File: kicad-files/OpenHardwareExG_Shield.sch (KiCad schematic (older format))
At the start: 189 parts, among them P1 CONN_1, P10 CONN_18, P11 CONN_1, P12 CONN_1, P13 CONN_1, P14 CONN_1, P15 CONN_1, P16 CONN_1, P17 CONN_1, P18 CONN_1, P19 ARDUINO_SHIELD, P2 CONN_1, P20 CONN_3X2, P21 CONN_3X2, P22 CONN_7, P23 CONN_1, P24 CONN_1, P25 CONN_1, P26 CONN_1, P27 CONN_1, P28 CONN_1, P29 CONN_1, P3 CONN_1, P30 CONN_1, P31 CONN_1, P32 CONN_1, P33 CONN_1, P34 CONN_1, P35 CONN_1, P36 CONN_1, P37 CONN_1, P38 CONN_1, P39 CONN_1, P4 CONN_1, P40 CONN_1, P41 CONN_1, P42 CONN_1, P43 CONN_1, P44 CONN_1, P45 CONN_1, P46 CONN_1, P47 CONN_1, P48 CONN_1, P49 CONN_1, P5 CONN_1, P50 CONN_1, P51 CONN_1, P52 CONN_1, P53 CONN_1, P54 CONN_1, P55 CONN_1, P6 CONN_1, P7 CONN_1, P8 CONN_1, P9 CONN_1, U1 ADS1299, U2 Z0109MNT1G, U3 TL431BIDBZR, U4 873-AAT3220IGY-33T1, U5 ADUM6000, U6 SI8663, U7 74LS02, U8 74LS00, U9 74LS125

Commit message: fix the crowbar on schematic
PCB still needs fixing
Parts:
- added C73: 330uF, ~, symbol CP
- C43: value 10uF -> 100nF
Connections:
- wire segments 765 -> 615
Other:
- note added: "5.5V Crowbar circuit"
- note removed: "3.8V Crowbar circuit"

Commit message: add footprint to 330uF C73
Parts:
- C73: footprint ~ -> c_tant_E

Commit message: T49D337K010ATE150 is a "D" footprint, not "E"
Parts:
- C73: footprint c_tant_E -> c_tant_D
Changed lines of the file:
@@
 Sheet 1 1
 Title ""
-Date "14 aug 2015"
+Date "30 aug 2015"
 Rev ""
 Comp ""
@@
 F 0 "C73" H 20750 1850 40  0000 L CNN
 F 1 "330uF" H 20750 1650 40  0000 L CNN
-F 2 "c_tant_E" H 20800 1600 30  0001 C CNN
+F 2 "c_tant_D" H 20800 1600 30  0001 C CNN
 F 3 "~" H 20700 1750 300 0000 C CNN
 	1    20700 1750

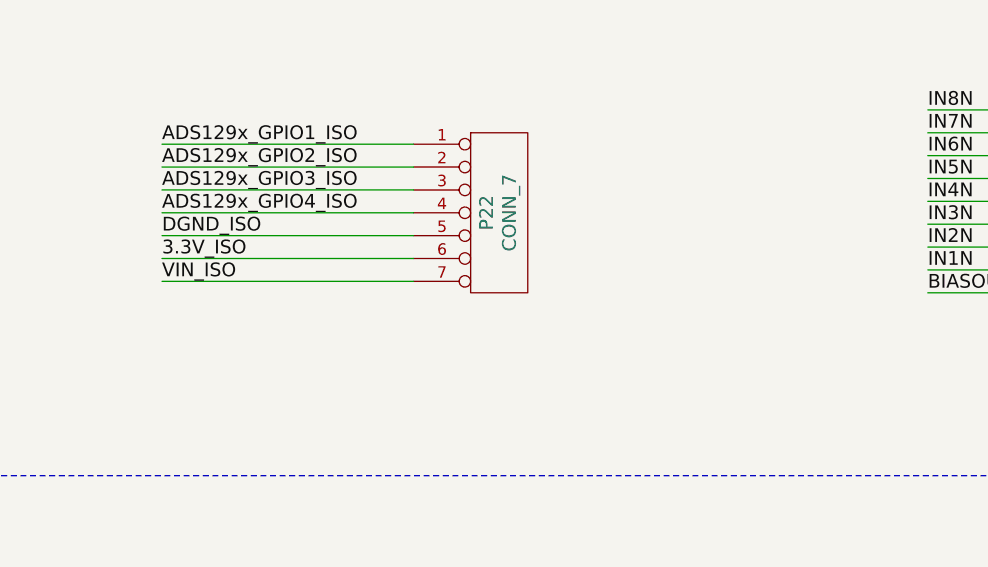
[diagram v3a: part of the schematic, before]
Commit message: add note to recommend female header for GPIO (P22)
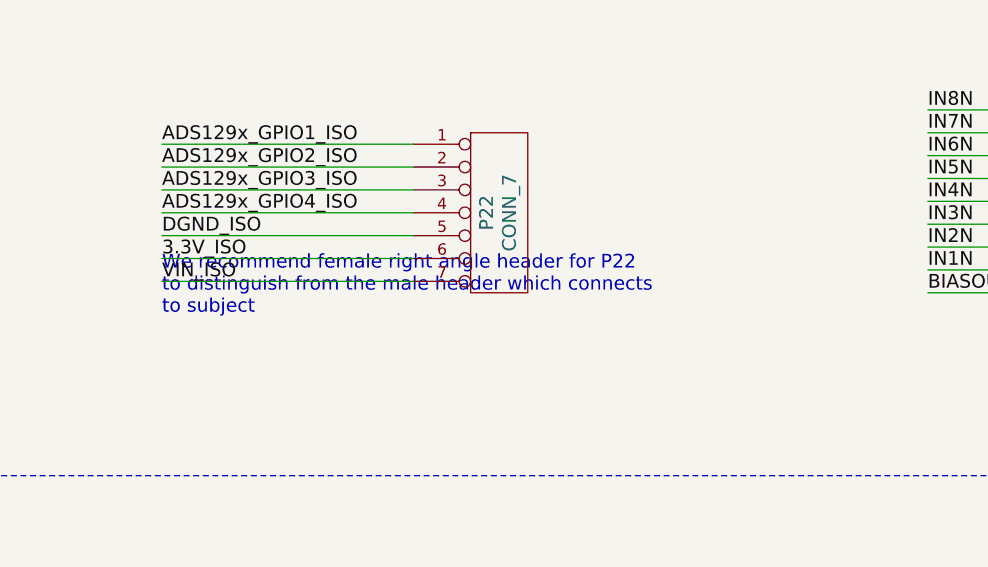
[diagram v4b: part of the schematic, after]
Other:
- note added: "We recommend female right angle header for P22\nto distinguish from the male header which connects\nto subject"
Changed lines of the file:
@@
 	20700 1950 20700 3000
 Connection ~ 20700 3000
+Text Notes 18850 10600 0    60   ~ 0
+We recommend female right angle header for P22\nto distinguish from the male header which connects\nto subject
 $EndSCHEMATC

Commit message: fix C43 footprint
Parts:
- C43: footprint SM0805 -> SM0603
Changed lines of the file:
@@
 F 0 "C43" H 15250 6900 50  0000 L CNN
 F 1 "100nF" H 15250 6700 50  0000 L CNN
-F 2 "SM0805" H 15250 6800 50  0001 C CNN
+F 2 "SM0603" H 15250 6800 50  0001 C CNN
 F 3 "" H 15200 6800 60  0001 C CNN
 	1    15200 6800

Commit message: connect DGND_ISO to DGND (DOH!); convert to KiCad 4
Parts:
- C1, C10, C11, C12, C13, C14, C15, C16, C17, C18, C19, C2, C20, C21, C22, C23, C24, C25, C26, C27, C28, C29, C3, C30, C31, C32, C33, C34, C35, C36, C37, C38, C39, C4, C40, C42, C43, C44, C45, C46, C47, C48, C49, C5, C50, C51, C52, C53, C54, C55, C56, C57, C58, C59, C6, C60, C61, C62, C63, C64, C65, C66, C67, C68, C69, C7, C70, C71, C72, C8, C9: symbol C -> C-RESCUE-OpenHardwareExG_Shield
- C41, C73: symbol CP -> CP-RESCUE-OpenHardwareExG_Shield
- D1: symbol LED -> LED-RESCUE-OpenHardwareExG_Shield
- R1, R10, R11, R12, R13, R14, R15, R16, R17, R18, R19, R2, R20, R21, R22, R23, R24, R25, R26, R27, R28, R29, R3, R30, R31, R32, R33, R34, R35, R36, R39, R4, R40, R41, R42, R43, R44, R45, R46, R5, R6, R7, R8, R9: symbol R -> R-RESCUE-OpenHardwareExG_Shield
- U5: symbol ADUM6000 -> ADuM6000
- U6: symbol SI8663 -> Si8663

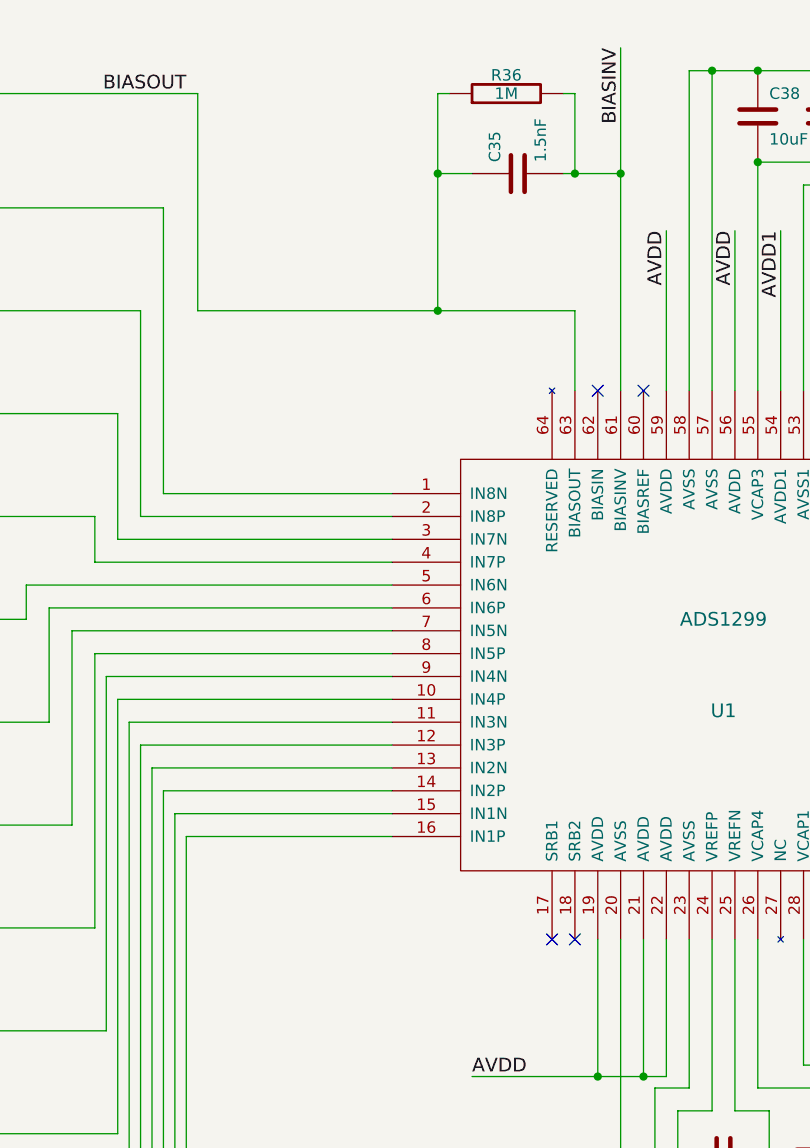
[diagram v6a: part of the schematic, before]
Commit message: add notes about connecting test points for next rev
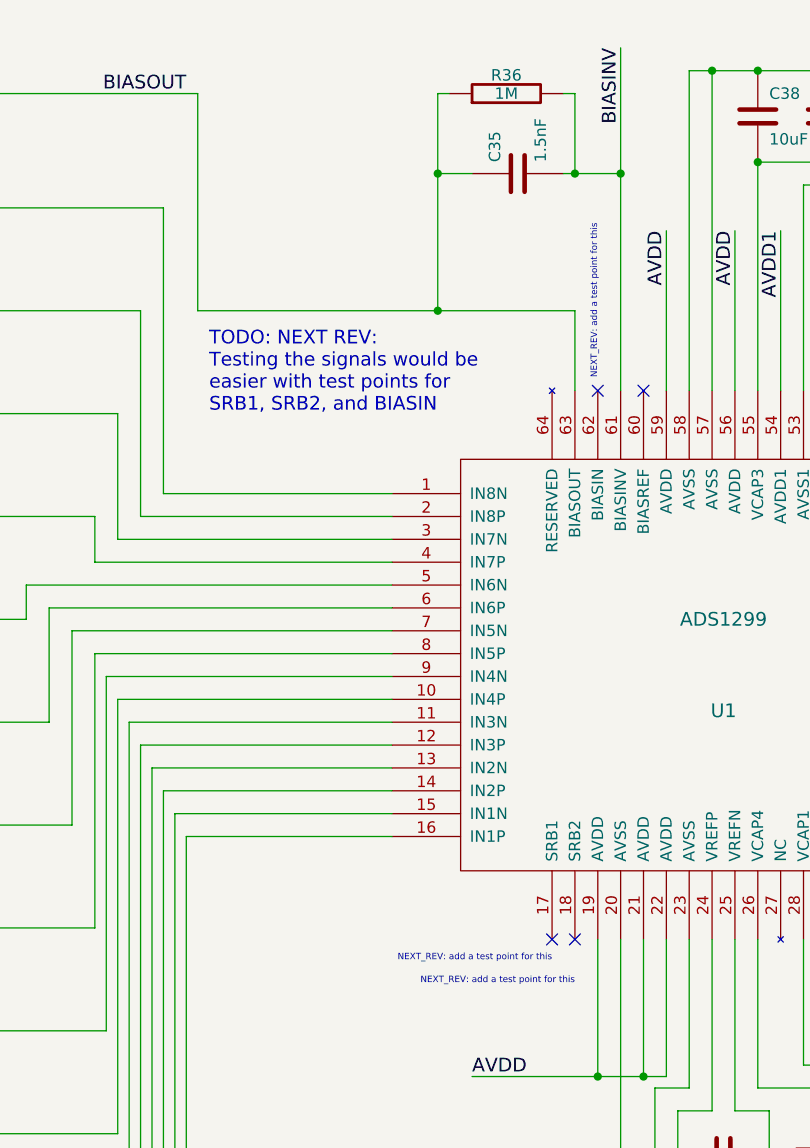
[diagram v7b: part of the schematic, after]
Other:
- note added: "NEXT_REV: add a test point for this"
- note added: "TODO: NEXT REV:\nTesting the signals would be\neasier with test points for\nSRB1, SRB2, and BIASIN"
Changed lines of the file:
@@
 Wire Wire Line
 	17750 7050 19750 7050
+Text Notes 10500 3150 1    28   ~ 0
+NEXT_REV: add a test point for this
+Text Notes 10300 5700 2    28   ~ 0
+NEXT_REV: add a test point for this
+Text Notes 10400 5800 2    28   ~ 0
+NEXT_REV: add a test point for this
+Text Notes 8800 3300 0    60   ~ 0
+TODO: NEXT REV:\nTesting the signals would be\neasier with test points for\nSRB1, SRB2, and BIASIN
 $EndSCHEMATC

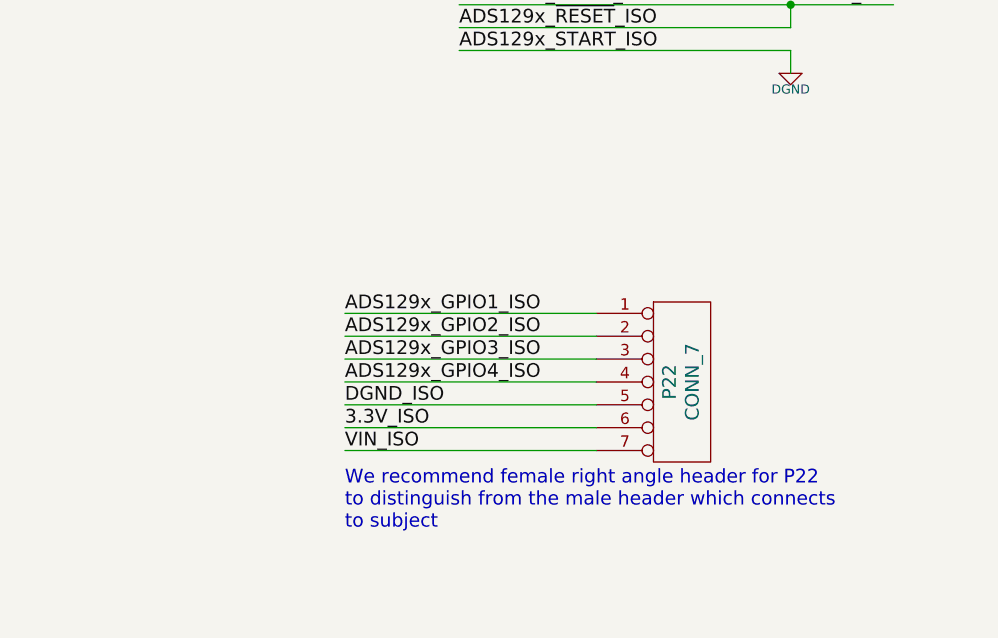
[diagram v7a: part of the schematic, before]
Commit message: add pulldown resistors for GPIOs
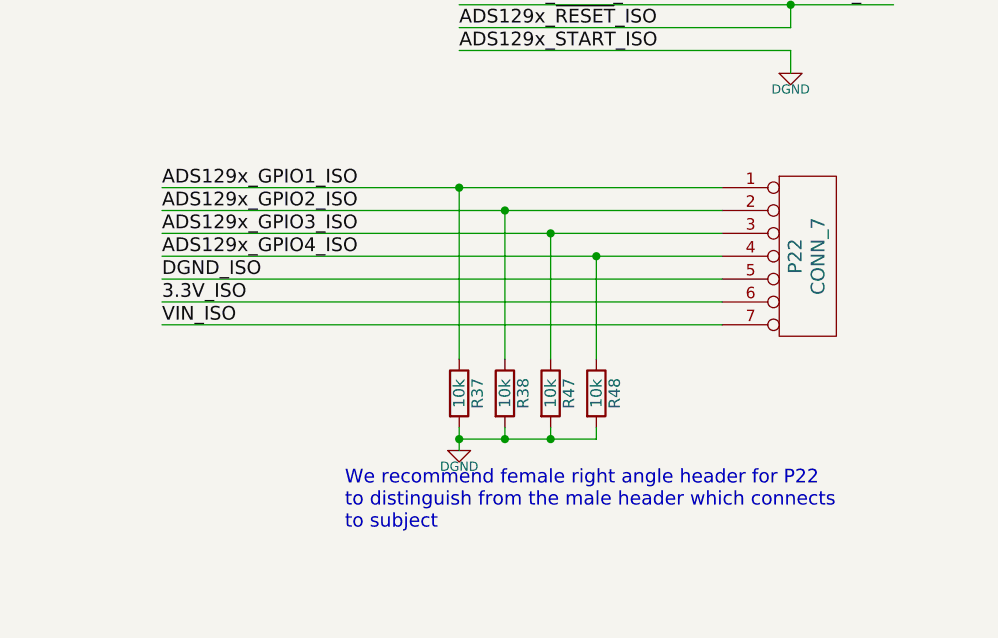
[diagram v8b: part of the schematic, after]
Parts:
- added R37, R38, R47, R48: 10k, Resistors_SMD:R_0603, symbol R
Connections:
- net ADS129x_GPIO1_ISO: now also R37.1
- net ADS129x_GPIO2_ISO: now also R38.1
- net ADS129x_GPIO3_ISO: now also R47.1
- net ADS129x_GPIO4_ISO: now also R48.1
- net AGND: now also R37.2, R38.2, R47.2, R48.2
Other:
- moved on the sheet: P22
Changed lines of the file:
@@
 Text Label 7300 19100 2    60   ~ 0
 MASTER_~DRDY~
-Text Label 18850 9850 0    60   ~ 0
+Text Label 18050 9300 0    60   ~ 0
 ADS129x_GPIO1_ISO
-Text Label 18850 10050 0    60   ~ 0
+Text Label 18050 9500 0    60   ~ 0
 ADS129x_GPIO3_ISO
-Text Label 18850 9950 0    60   ~ 0
+Text Label 18050 9400 0    60   ~ 0
 ADS129x_GPIO2_ISO
-Text Label 18850 10150 0    60   ~ 0
+Text Label 18050 9600 0    60   ~ 0
 ADS129x_GPIO4_ISO
-Text Label 18850 10450 0    60   ~ 0
+Text Label 18050 9900 0    60   ~ 0
 VIN_ISO
 Text Label 10600 1700 3    60   ~ 0
@@
 	1    0    0    1
 $EndComp
-Text Label 18850 10350 0    60   ~ 0
+Text Label 18050 9800 0    60   ~ 0
 3.3V_ISO
 $Comp
@@
 	1    0    0    1
 $EndComp
-Text Label 18850 10250 0    60   ~ 0
+Text Label 18050 9700 0    60   ~ 0
 DGND_ISO
 $Comp
@@
 L CONN_7 P22
 U 1 1 54C521DD
-P 20300 10150
-F 0 "P22" V 20270 10150 60  0000 C CNN
-F 1 "CONN_7" V 20370 10150 60  0000 C CNN
-F 2 "PIN_ARRAY_7x1" H 20300 10150 60  0001 C CNN
-F 3 "" H 20300 10150 60  0000 C CNN
-	1    20300 10150
+P 20850 9600
+F 0 "P22" V 20820 9600 60  0000 C CNN
+F 1 "CONN_7" V 20920 9600 60  0000 C CNN
+F 2 "PIN_ARRAY_7x1" H 20850 9600 60  0001 C CNN
+F 3 "" H 20850 9600 60  0000 C CNN
+	1    20850 9600
 	1    0    0    -1
 $EndComp
@@
 	7300 19100 6000 19100
 Wire Wire Line
-	18850 9850 19950 9850
-Wire Wire Line
-	19950 9950 18850 9950
-Wire Wire Line
-	18850 10050 19950 10050
-Wire Wire Line
-	19950 10150 18850 10150
-Wire Wire Line
-	18850 10450 19950 10450
-Wire Wire Line
-	18850 10250 19950 10250
+	18050 9300 20500 9300
+Wire Wire Line
+	20500 9400 18050 9400
+Wire Wire Line
+	18050 9500 20500 9500
+Wire Wire Line
+	20500 9600 18050 9600
+Wire Wire Line
+	18050 9900 20500 9900
+Wire Wire Line
+	18050 9700 20500 9700
 Wire Wire Line
 	9800 1900 9800 2850
@@
 	25400 7500 27000 7500
 Wire Wire Line
-	19950 10350 18850 10350
+	20500 9800 18050 9800
 Wire Wire Line
 	13700 10400 13700 10500
@@
 Text Notes 8800 3300 0    60   ~ 0
 TODO: NEXT REV:\nTesting the signals would be\neasier with test points for\nSRB1, SRB2, and BIASIN
+$Comp
+L R R37
+U 1 1 57C693A4
+P 19350 10200
+F 0 "R37" V 19430 10200 50  0000 C CNN
+F 1 "10k" V 19350 10200 50  0000 C CNN
+F 2 "Resistors_SMD:R_0603" V 19280 10200 50  0001 C CNN
+F 3 "" H 19350 10200 50  0000 C CNN
+	1    19350 10200
+	1    0    0    -1
+$EndComp
+$Comp
+L R R38
+U 1 1 57C69551
+P 19550 10200
+F 0 "R38" V 19630 10200 50  0000 C CNN
+F 1 "10k" V 19550 10200 50  0000 C CNN
+F 2 "Resistors_SMD:R_0603" V 19480 10200 50  0001 C CNN
+F 3 "" H 19550 10200 50  0000 C CNN
+	1    19550 10200
+	1    0    0    -1
+$EndComp
+$Comp
+L R R47
+U 1 1 57C696F2
+P 19750 10200
+F 0 "R47" V 19830 10200 50  0000 C CNN
+F 1 "10k" V 19750 10200 50  0000 C CNN
+F 2 "Resistors_SMD:R_0603" V 19680 10200 50  0001 C CNN
+F 3 "" H 19750 10200 50  0000 C CNN
+	1    19750 10200
+	1    0    0    -1
+$EndComp
+$Comp
+L R R48
+U 1 1 57C69AFA
+P 19950 10200
+F 0 "R48" V 20030 10200 50  0000 C CNN
+F 1 "10k" V 19950 10200 50  0000 C CNN
+F 2 "Resistors_SMD:R_0603" V 19880 10200 50  0001 C CNN
+F 3 "" H 19950 10200 50  0000 C CNN
+	1    19950 10200
+	1    0    0    -1
+$EndComp
+$Comp
+L DGND #PWR087
+U 1 1 57C6A2F3
+P 19350 10450
+F 0 "#PWR087" H 19350 10450 40  0001 C CNN
+F 1 "DGND" H 19350 10380 40  0000 C CNN
+F 2 "" H 19350 10450 60  0000 C CNN
+F 3 "" H 19350 10450 60  0000 C CNN
+	1    19350 10450
+	1    0    0    -1
+$EndComp
+Wire Wire Line
+	19350 10450 19350 10350
+Wire Wire Line
+	19350 10400 19950 10400
+Wire Wire Line
+	19550 10400 19550 10350
+Connection ~ 19350 10400
+Wire Wire Line
+	19750 10400 19750 10350
+Connection ~ 19550 10400
+Wire Wire Line
+	19950 10400 19950 10350
+Connection ~ 19750 10400
+Wire Wire Line
+	19350 10050 19350 9300
+Connection ~ 19350 9300
+Wire Wire Line
+	19550 10050 19550 9400
+Connection ~ 19550 9400
+Wire Wire Line
+	19750 10050 19750 9500
+Connection ~ 19750 9500
+Wire Wire Line
+	19950 10050 19950 9600
+Connection ~ 19950 9600
 $EndSCHEMATC
